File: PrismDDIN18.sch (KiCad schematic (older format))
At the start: 86 parts, among them CON1 BARREL_JACK, IC1 LM2596T-5, J1 Conn_01x03, M1 IN-18, M10 IN-18, Q2 2N7000, Q3 2N7000, Q4 2N7000, Q5 2N7000, Q6 IRF540N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

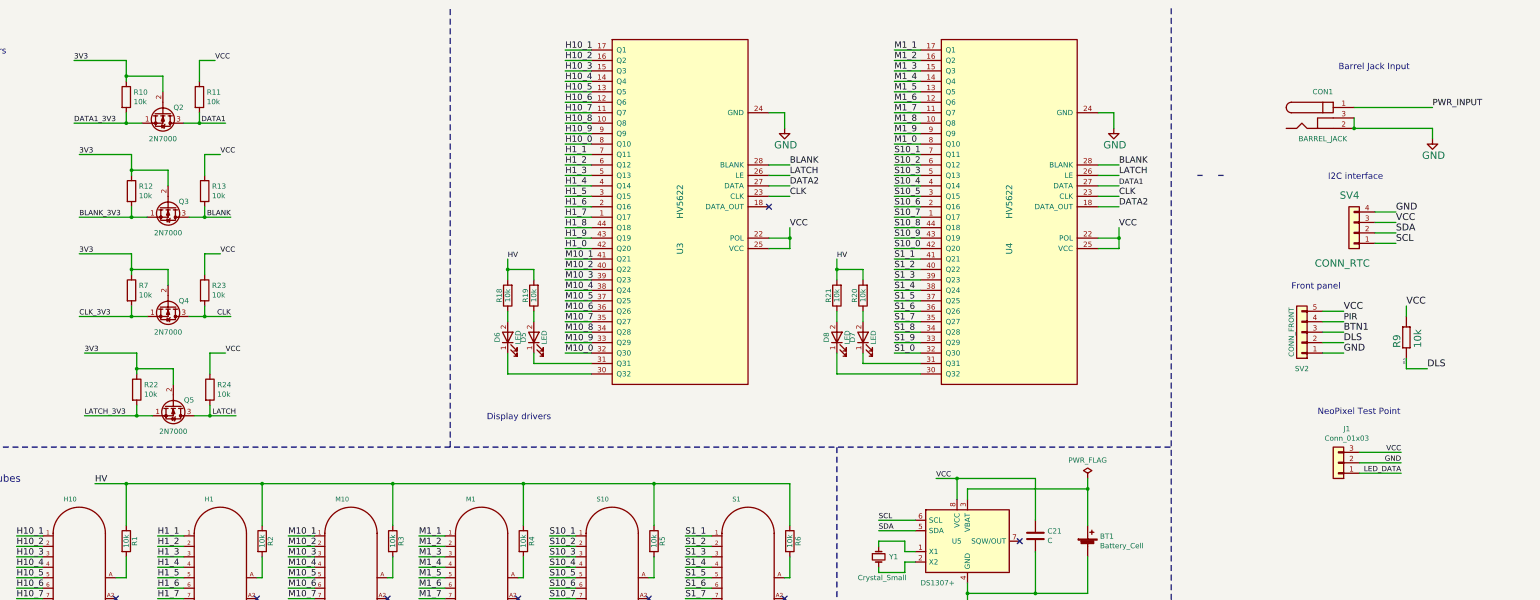
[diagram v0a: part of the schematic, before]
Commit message: Improve VCC and HV layout
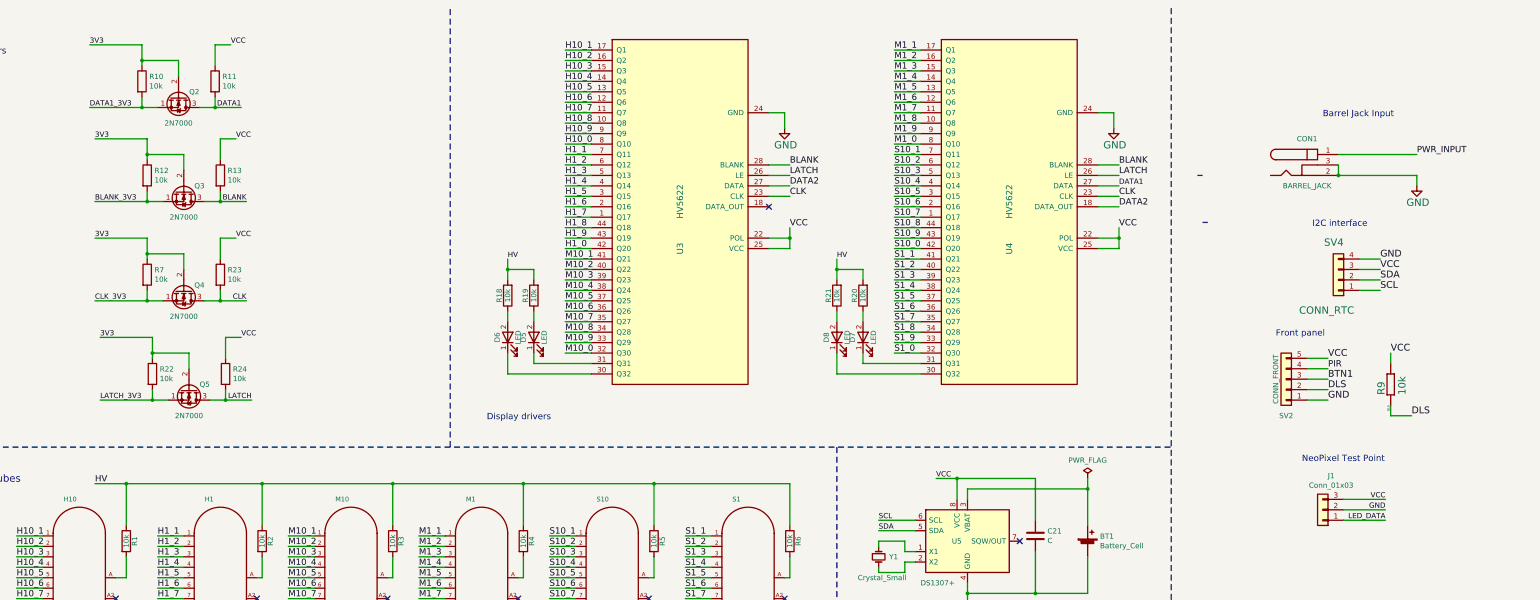
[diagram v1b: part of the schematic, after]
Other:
- moved on the sheet: CON1, J1, Q2, Q3, Q4, Q5, R10, R11, R12, R13, R22, R23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

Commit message: More minor improvements
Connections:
- net 3V3: now also SV4.3 (Pin_3)
- net VCC: no longer SV4.3 (Pin_3)
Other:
- note added: "I2C interface (3V3)"
- note removed: "I2C interface"
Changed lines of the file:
@@
 VCC
 Text Label 14600 3000 0    65   ~ 0
-VCC
+3V3
 Text Label 14100 3850 0    65   ~ 0
 VCC
@@
 Display drivers
 Text Notes 13950 2600 0    60   ~ 0
-I2C interface
+I2C interface (3V3)
 Text Notes 13600 3650 0    60   ~ 0
 Front panel

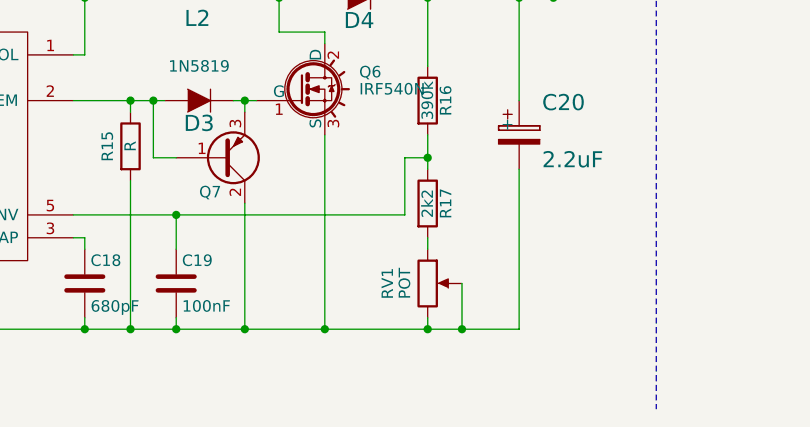
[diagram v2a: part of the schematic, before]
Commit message: Update IN-18 footprints, define RV1 value
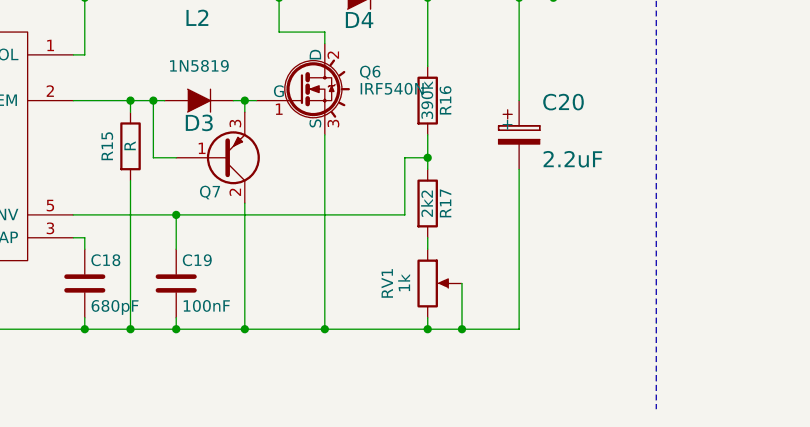
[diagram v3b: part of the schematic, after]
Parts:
- H1, H10, M1, M10, S1, S10: footprint russian-nixies:russian-nixies-IN-18 -> NixieClockMaster:IN-18
- Q2, Q3, Q4, Q5: footprint Package_TO_SOT_THT:TO-92_Inline -> NixieClockMaster:TO-92_inline_2N7000
- Q6: footprint Power_Integrations:TO-220 -> NixieClockMaster:TO-220-3_H
- R1: footprint NixieClockMaster:R-0207_2V -> NixieClockMaster:R_Short_P7.62mm_Horizontal
- RV1: value POT -> 1k; footprint Potentiometers:Potentiometer_Bourns_3296W_3-8Zoll_Inline_ScrewUp -> NixieClockMaster:Potentiometer_Trimmer_Bourns_3296X
- U2: footprint Housings_DIP:DIP-8_W7.62mm_LongPads -> NixieClockMaster:MC34063_DIL8
- U5: footprint Package_DIP:DIP-8_W7.62mm -> NixieClockMaster:DS1307_DIL8
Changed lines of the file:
@@
 F 0 "S10" H 7100 6875 45  0000 L BNN
 F 1 "IN-18" H 7300 6050 45  0001 L BNN
-F 2 "russian-nixies:russian-nixies-IN-18" H 7300 6050 60  0001 C CNN
+F 2 "NixieClockMaster:IN-18" H 7300 6050 60  0001 C CNN
 F 3 "" H 7300 6050 60  0001 C CNN
 	1    7300 6050
@@
 F 0 "M1" H 5850 6875 45  0000 L BNN
 F 1 "IN-18" H 6050 6050 45  0001 L BNN
-F 2 "russian-nixies:russian-nixies-IN-18" H 6050 6050 60  0001 C CNN
+F 2 "NixieClockMaster:IN-18" H 6050 6050 60  0001 C CNN
 F 3 "" H 6050 6050 60  0001 C CNN
 	1    6050 6050
@@
 F 0 "M10" H 4600 6875 45  0000 L BNN
 F 1 "IN-18" H 4800 6050 45  0001 L BNN
-F 2 "russian-nixies:russian-nixies-IN-18" H 4800 6050 60  0001 C CNN
+F 2 "NixieClockMaster:IN-18" H 4800 6050 60  0001 C CNN
 F 3 "" H 4800 6050 60  0001 C CNN
 	1    4800 6050
@@
 F 0 "S1" H 8400 6875 45  0000 L BNN
 F 1 "IN-18" H 8600 6050 45  0001 L BNN
-F 2 "russian-nixies:russian-nixies-IN-18" H 8600 6050 60  0001 C CNN
+F 2 "NixieClockMaster:IN-18" H 8600 6050 60  0001 C CNN
 F 3 "" H 8600 6050 60  0001 C CNN
 	1    8600 6050
@@
 F 0 "H10" H 2000 6875 45  0000 L BNN
 F 1 "IN-18" H 2200 6050 45  0001 L BNN
-F 2 "russian-nixies:russian-nixies-IN-18" H 2200 6050 60  0001 C CNN
+F 2 "NixieClockMaster:IN-18" H 2200 6050 60  0001 C CNN
 F 3 "" H 2200 6050 60  0001 C CNN
 	1    2200 6050
@@
 F 0 "H1" H 3350 6875 45  0000 L BNN
 F 1 "IN-18" H 3550 6050 45  0001 L BNN
-F 2 "russian-nixies:russian-nixies-IN-18" H 3550 6050 60  0001 C CNN
+F 2 "NixieClockMaster:IN-18" H 3550 6050 60  0001 C CNN
 F 3 "" H 3550 6050 60  0001 C CNN
 	1    3550 6050
@@
 F 0 "R1" V 2680 5600 50  0000 C CNN
 F 1 "10k" V 2600 5600 50  0000 C CNN
-F 2 "NixieClockMaster:R-0207_2V" V 2530 5600 50  0001 C CNN
+F 2 "NixieClockMaster:R_Short_P7.62mm_Horizontal" V 2530 5600 50  0001 C CNN
 F 3 "" H 2600 5600 50  0000 C CNN
 	1    2600 5600
@@
 F 0 "U2" H 7900 10600 60  0000 L CNN
 F 1 "MC34063A" H 8100 10050 60  0000 L CNN
-F 2 "Housings_DIP:DIP-8_W7.62mm_LongPads" H 8200 9550 60  0001 C CNN
+F 2 "NixieClockMaster:MC34063_DIL8" H 8200 9550 60  0001 C CNN
 F 3 "" H 8200 9550 60  0000 C CNN
 	1    8200 10050
@@
 P 10450 10650
 F 0 "RV1" V 10275 10650 50  0000 C CNN
-F 1 "POT" V 10350 10650 50  0000 C CNN
-F 2 "Potentiometers:Potentiometer_Bourns_3296W_3-8Zoll_Inline_ScrewUp" H 10450 10650 50  0001 C CNN
+F 1 "1k" V 10350 10650 50  0000 C CNN
+F 2 "NixieClockMaster:Potentiometer_Trimmer_Bourns_3296X" H 10450 10650 50  0001 C CNN
 F 3 "" H 10450 10650 50  0000 C CNN
 	1    10450 10650
@@
 F 0 "Q6" H 10150 9875 50  0000 L CNN
 F 1 "IRF540N" H 10150 9800 50  0000 L CNN
-F 2 "Power_Integrations:TO-220" H 10150 9725 50  0001 L CIN
+F 2 "NixieClockMaster:TO-220-3_H" H 10150 9725 50  0001 L CIN
 F 3 "" H 9900 9800 50  0000 L CNN
 	1    9900 9800
@@
 F 0 "U5" H 10500 5600 50  0000 L CNN
 F 1 "DS1307+" H 10200 5200 50  0000 L CNN
-F 2 "Package_DIP:DIP-8_W7.62mm" H 10650 5100 50  0001 C CNN
+F 2 "NixieClockMaster:DS1307_DIL8" H 10650 5100 50  0001 C CNN
 F 3 "https://datasheets.maximintegrated.com/en/ds/DS1307.pdf" H 10650 5400 50  0001 C CNN
 	1    10650 5600
@@
 F 0 "Q2" V 3050 1500 50  0000 C CNN
 F 1 "2N7000" V 3350 1350 50  0000 C CNN
-F 2 "Package_TO_SOT_THT:TO-92_Inline" H 3300 1275 50  0001 L CIN
+F 2 "NixieClockMaster:TO-92_inline_2N7000" H 3300 1275 50  0001 L CIN
 F 3 "https://www.fairchildsemi.com/datasheets/2N/2N7000.pdf" H 3100 1350 50  0001 L CNN
 	1    3100 1350
@@
 F 0 "Q3" V 3100 2400 50  0000 C CNN
 F 1 "2N7000" V 3400 2250 50  0000 C CNN
-F 2 "Package_TO_SOT_THT:TO-92_Inline" H 3350 2175 50  0001 L CIN
+F 2 "NixieClockMaster:TO-92_inline_2N7000" H 3350 2175 50  0001 L CIN
 F 3 "https://www.fairchildsemi.com/datasheets/2N/2N7000.pdf" H 3150 2250 50  0001 L CNN
 	1    3150 2250
@@
 F 0 "Q4" V 3100 3350 50  0000 C CNN
 F 1 "2N7000" V 3400 3200 50  0000 C CNN
-F 2 "Package_TO_SOT_THT:TO-92_Inline" H 3350 3125 50  0001 L CIN
+F 2 "NixieClockMaster:TO-92_inline_2N7000" H 3350 3125 50  0001 L CIN
 F 3 "https://www.fairchildsemi.com/datasheets/2N/2N7000.pdf" H 3150 3200 50  0001 L CNN
 	1    3150 3200
@@
 F 0 "Q5" V 3150 4300 50  0000 C CNN
 F 1 "2N7000" V 3450 4150 50  0000 C CNN
-F 2 "Package_TO_SOT_THT:TO-92_Inline" H 3400 4075 50  0001 L CIN
+F 2 "NixieClockMaster:TO-92_inline_2N7000" H 3400 4075 50  0001 L CIN
 F 3 "https://www.fairchildsemi.com/datasheets/2N/2N7000.pdf" H 3200 4150 50  0001 L CNN
 	1    3200 4150

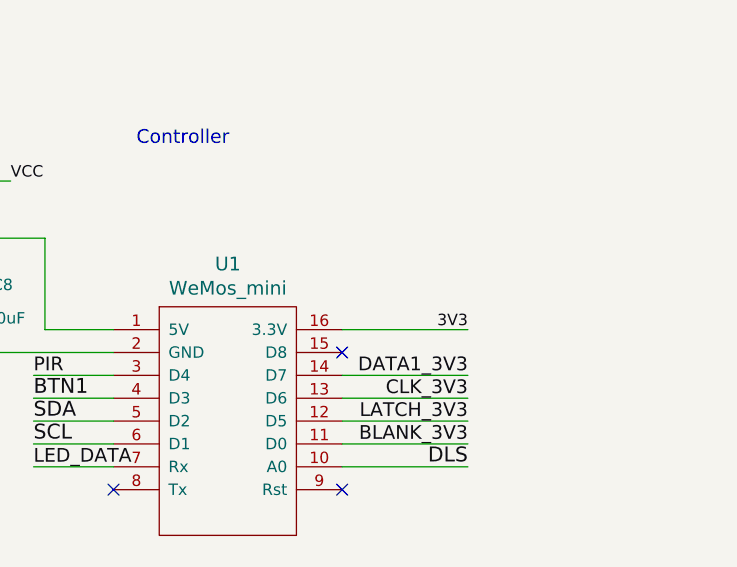
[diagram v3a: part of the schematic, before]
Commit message: Add 3V3 test point, move test points
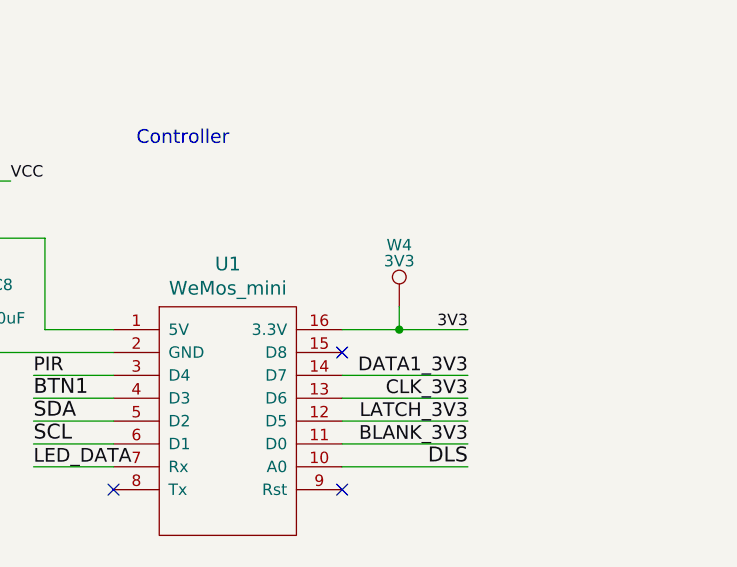
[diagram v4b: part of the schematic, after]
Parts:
- added W4: 3V3, NixieClockMaster:TESTPAD_P1-13, symbol PrismDDIN18-rescue:TEST_1P
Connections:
- net 3V3: now also W4.1
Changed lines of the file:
@@
 	12750 8450 12750 8300
 Wire Wire Line
-	14400 8200 14950 8200
+	14400 8200 14650 8200
 Wire Wire Line
 	14400 8400 14950 8400
@@
 Text Notes 13500 7400 0    60   ~ 0
 Controller
+$Comp
+L PrismDDIN18-rescue:TEST_1P W4
+U 1 1 5C15B1F7
+P 14650 8100
+F 0 "W4" H 14650 8370 50  0000 C CNN
+F 1 "3V3" H 14650 8300 50  0000 C CNN
+F 2 "NixieClockMaster:TESTPAD_P1-13" H 14850 8100 50  0001 C CNN
+F 3 "" H 14850 8100 50  0000 C CNN
+	1    14650 8100
+	1    0    0    -1
+$EndComp
+Wire Wire Line
+	14650 8100 14650 8200
+Connection ~ 14650 8200
+Wire Wire Line
+	14650 8200 14950 8200
 $EndSCHEMATC

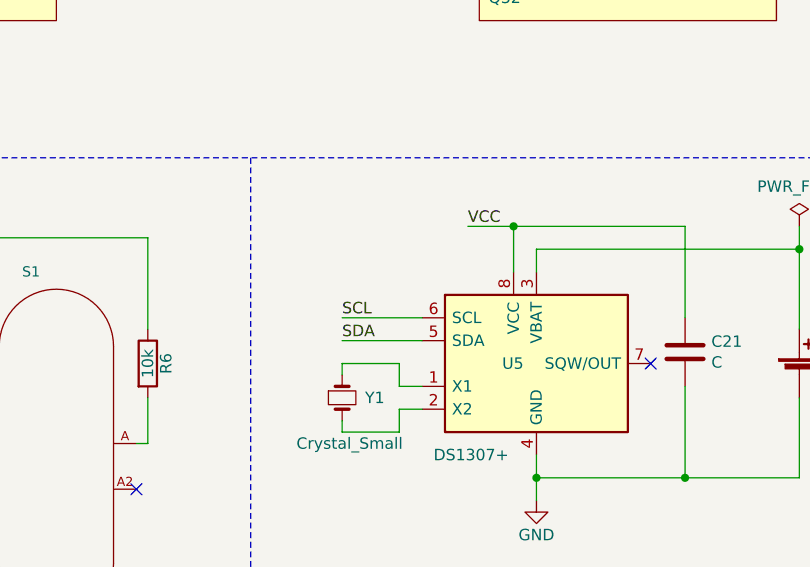
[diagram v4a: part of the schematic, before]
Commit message: Add I2C pullups
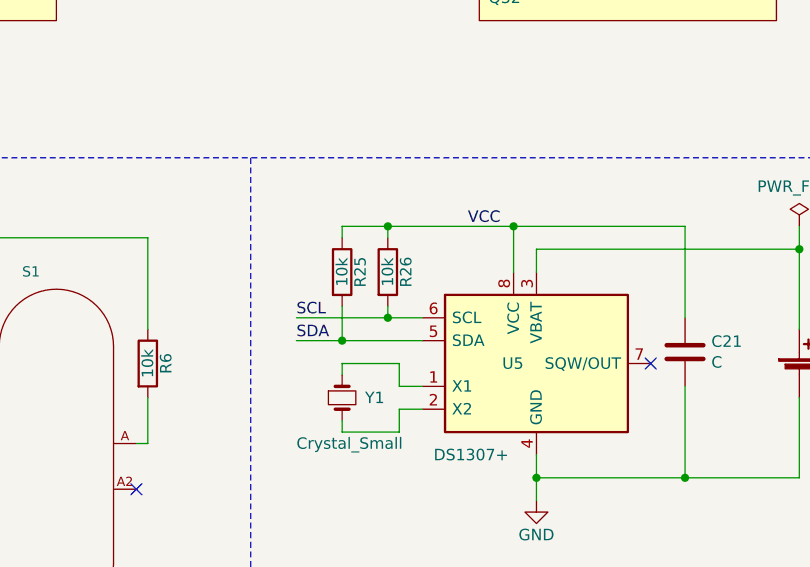
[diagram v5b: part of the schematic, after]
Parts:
- added R25, R26: 10k, NixieClockMaster:R-0207_2V, symbol PrismDDIN18-rescue:R
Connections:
- net SCL: now also R26.2
- net SDA: now also R25.2
- net VCC: now also R25.1, R26.1
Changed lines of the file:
@@
 Wire Wire Line
 	9800 5900 9800 5850
-Wire Wire Line
-	10150 5400 9800 5400
-Wire Wire Line
-	10150 5500 9800 5500
-Text Label 9800 5400 0    50   ~ 0
+Text Label 9600 5400 0    50   ~ 0
 SCL
-Text Label 9800 5500 0    50   ~ 0
+Text Label 9600 5500 0    50   ~ 0
 SDA
 $Comp
@@
 Wire Wire Line
 	10550 5000 10550 5200
-Wire Wire Line
-	10550 5000 10350 5000
 Connection ~ 10550 5000
 Text Label 10350 5000 0    50   ~ 0
@@
 Wire Wire Line
 	14650 8200 14950 8200
+$Comp
+L PrismDDIN18-rescue:R R25
+U 1 1 5C2469EC
+P 9800 5200
+F 0 "R25" V 9880 5200 50  0000 C CNN
+F 1 "10k" V 9800 5200 50  0000 C CNN
+F 2 "NixieClockMaster:R-0207_2V" V 9730 5200 50  0001 C CNN
+F 3 "" H 9800 5200 50  0000 C CNN
+	1    9800 5200
+	1    0    0    -1
+$EndComp
+$Comp
+L PrismDDIN18-rescue:R R26
+U 1 1 5C246B2E
+P 10000 5200
+F 0 "R26" V 10080 5200 50  0000 C CNN
+F 1 "10k" V 10000 5200 50  0000 C CNN
+F 2 "NixieClockMaster:R-0207_2V" V 9930 5200 50  0001 C CNN
+F 3 "" H 10000 5200 50  0000 C CNN
+	1    10000 5200
+	1    0    0    -1
+$EndComp
+Wire Wire Line
+	9600 5400 10000 5400
+Wire Wire Line
+	9600 5500 9800 5500
+Wire Wire Line
+	9800 5350 9800 5500
+Connection ~ 9800 5500
+Wire Wire Line
+	9800 5500 10150 5500
+Wire Wire Line
+	10000 5350 10000 5400
+Connection ~ 10000 5400
+Wire Wire Line
+	10000 5400 10150 5400
+Wire Wire Line
+	10000 5000 10000 5050
+Wire Wire Line
+	10000 5000 10550 5000
+Wire Wire Line
+	10000 5000 9800 5000
+Wire Wire Line
+	9800 5000 9800 5050
+Connection ~ 10000 5000
 $EndSCHEMATC

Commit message: Correct 2N3906 pin out
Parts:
- Q7: symbol PrismDDIN18-rescue:Q_PNP_BCE -> Device:Q_PNP_CBE
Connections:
- net GND: now also Q7.1 (C); no longer Q7.2 (C)
- net at D3.2 (A), R15.1, U2.2 (SWEM): now also Q7.2 (B); no longer Q7.1 (B)
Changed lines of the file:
@@
 Connection ~ 9150 9850
 $Comp
-L PrismDDIN18-rescue:Q_PNP_BCE Q7
+L Device:Q_PNP_CBE Q7
 U 1 1 5937A70F
 P 9550 10100

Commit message: Update component values
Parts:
- C12: value 220uF -> 220uF 10V
- C16, C17: value 220uF -> 220uF 35V
- C20: value 2.2uF -> 2.2uF 400V
- C21: value C -> 100nF
- R15: value R -> 1k
- U1: symbol NixieClockMaster:WeMos_mini -> PrismDDIN18-rescue:WeMos_mini-NixieClockMaster
- Y1: value Crystal_Small -> 32.768kHz
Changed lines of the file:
@@
 U 1 1 59345978
 P 2400 10500
-F 0 "C11" H 2460 10515 70  0000 L BNN
+F 0 "C11" H 2200 10300 70  0000 L BNN
 F 1 "100nF" H 2050 10500 70  0000 L BNN
 F 2 "NixieClockMaster:C025-024X044" H 2390 10290 70  0001 L TNN
@@
 P 4450 10200
 F 0 "C12" H 4500 10050 70  0000 L BNN
-F 1 "220uF" V 4400 9800 70  0000 L BNN
+F 1 "220uF 10V" V 4400 9800 70  0000 L BNN
 F 2 "NixieClockMaster:C_Radial_D6.3_L11.2_P2.5" H 4440 9990 70  0001 L TNN
 F 3 "" H 4450 10200 60  0001 C CNN
@@
 U 1 1 5934C6FD
 P 1900 10450
-F 0 "C16" H 2000 10550 70  0000 L BNN
-F 1 "220uF" H 1550 10300 70  0000 L BNN
+F 0 "C16" H 1650 10300 70  0000 L BNN
+F 1 "220uF 35V" H 1600 10000 70  0000 L BNN
 F 2 "NixieClockMaster:C_Radial_D6.3_L11.2_P2.5" H 1890 10240 70  0001 L TNN
 F 3 "" H 1900 10450 60  0001 C CNN
@@
 P 7400 10450
 F 0 "C17" H 7500 10550 70  0000 L BNN
-F 1 "220uF" H 7050 10300 70  0000 L BNN
+F 1 "220uF 35V" H 6950 10100 70  0000 L BNN
 F 2 "NixieClockMaster:C_Radial_D6.3_L11.2_P2.5" H 7390 10240 70  0001 L TNN
 F 3 "" H 7400 10450 60  0001 C CNN
@@
 P 9150 10050
 F 0 "R15" V 9050 10050 50  0000 C CNN
-F 1 "R" V 9150 10050 50  0000 C CNN
+F 1 "1k" V 9150 10050 50  0000 C CNN
 F 2 "NixieClockMaster:R-0207_2V" V 9080 10050 50  0001 C CNN
 F 3 "" H 9150 10050 50  0000 C CNN
@@
 P 10850 10000
 F 0 "C20" H 10950 10100 70  0000 L BNN
-F 1 "2.2uF" H 10950 9850 70  0000 L BNN
+F 1 "2.2uF 400V" H 10950 9850 70  0000 L BNN
 F 2 "NixieClockMaster:C_Radial_D6.3_L11.2_P2.5" H 10840 9790 70  0001 L TNN
 F 3 "" H 10850 10000 60  0001 C CNN
@@
 P 9800 5750
 F 0 "Y1" V 9800 5850 50  0000 L CNN
-F 1 "Crystal_Small" V 10000 5550 50  0000 L CNN
+F 1 "32.768kHz" V 10000 5550 50  0000 L CNN
 F 2 "NixieClockMaster:Crystal_DS10_d1.0mm_l4.3mm_Horizontal" H 9800 5750 50  0001 C CNN
 F 3 "~" H 9800 5750 50  0001 C CNN
@@
 P 11300 5550
 F 0 "C21" H 11415 5596 50  0000 L CNN
-F 1 "C" H 11415 5505 50  0000 L CNN
+F 1 "100nF" H 11415 5505 50  0000 L CNN
 F 2 "NixieClockMaster:C025-024X044" H 11338 5400 50  0001 C CNN
 F 3 "~" H 11300 5550 50  0001 C CNN
@@
 	9400 4700 9400 7000
 $Comp
-L NixieClockMaster:WeMos_mini U1
+L PrismDDIN18-rescue:WeMos_mini-NixieClockMaster U1
 U 1 1 5C458A48
 P 13900 8550
